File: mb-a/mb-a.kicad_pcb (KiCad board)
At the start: 2 copper layers, 39 x 56 mm, 29 parts, among them J1 Power, J2 Speaker, M1 Orange-Pi-Zero, U1 NCP1117-5.0_SOT223, U2 PAM8320, X1 I2C-6P

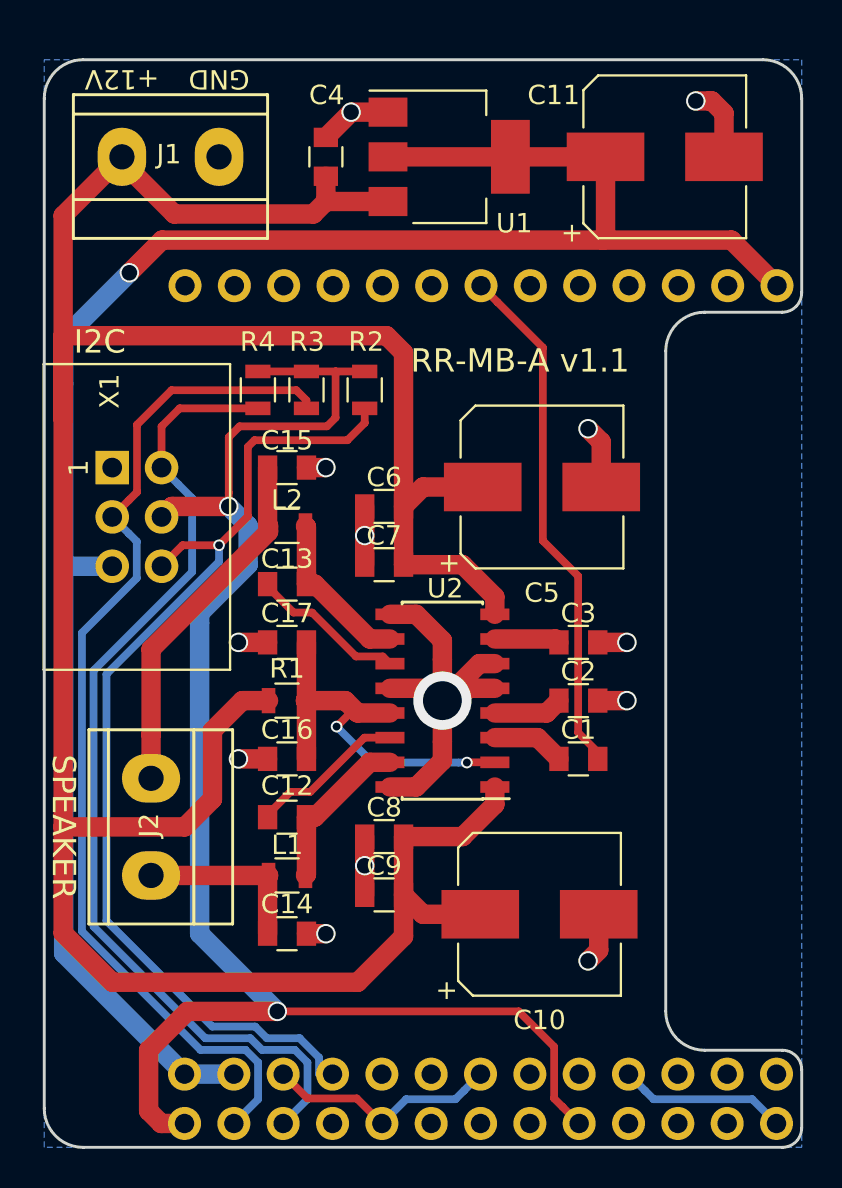
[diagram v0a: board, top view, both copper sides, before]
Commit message: Band switch support
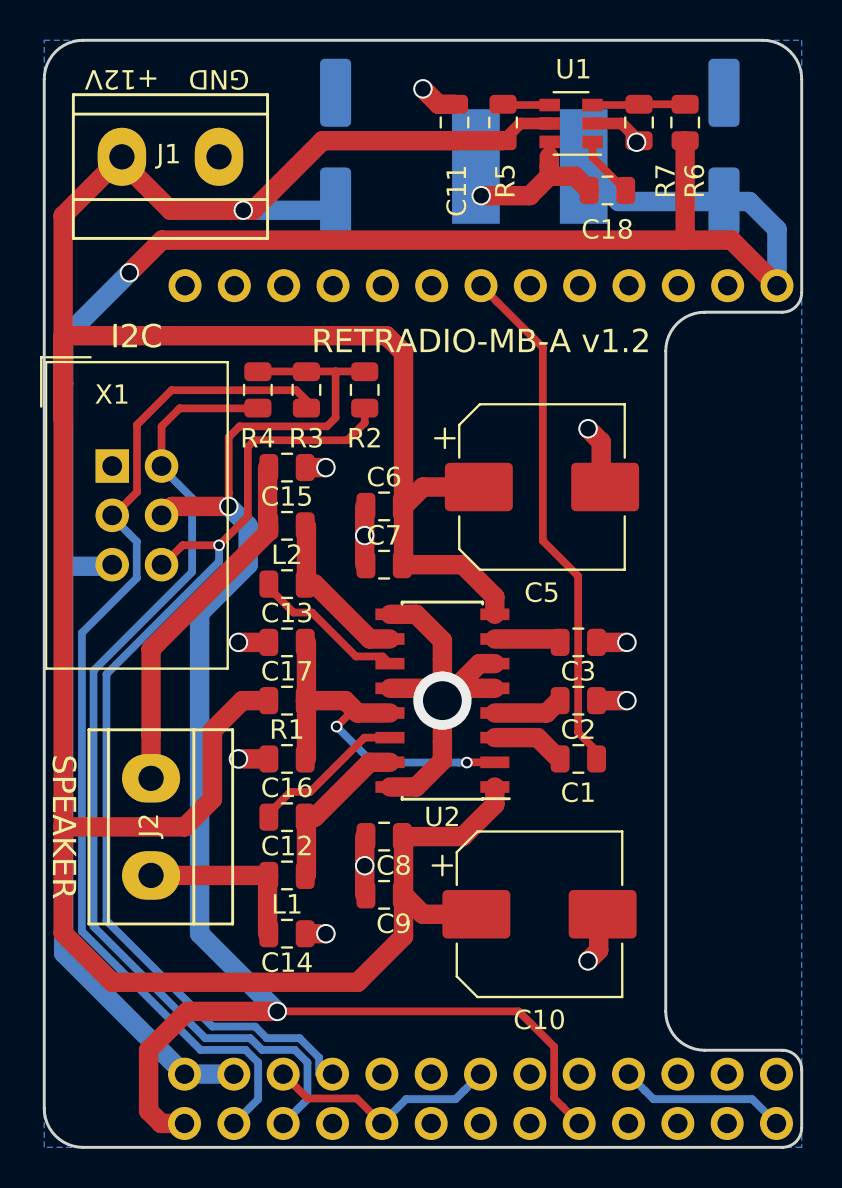
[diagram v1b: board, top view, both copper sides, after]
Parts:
- added C18: 100n, Capacitor_SMD:C_0805_2012Metric, F.Cu at (120.5, 46.7)
- added C19: 100u/12V, Capacitor_SMD:CP_Elec_6.3x5.4, B.Cu at (126.5, 44.5)
- added L3: 6.8uH, mb-a:L_Taiyo-Yuden_NR-60xx_HandSoldering, B.Cu at (116.5, 45.5)
- added R5: 100k, Resistor_SMD:R_0805_2012Metric, F.Cu at (115.1, 43.2)
- added R6: 30.9k 1%, Resistor_SMD:R_0805_2012Metric, F.Cu at (124.5, 43.2)
- added R7: 4.22k 1%, Resistor_SMD:R_0805_2012Metric, F.Cu at (122.1, 43.2)
- C1, C12, C13, C14, C15, C16, C17, C2, C3, C6, C7, C8, C9: footprint Capacitors_SMD:C_0805 -> Capacitor_SMD:C_0805_2012Metric
- C10, C5: footprint Capacitors_SMD:CP_Elec_8x10 -> Capacitor_SMD:CP_Elec_8x10
- C11: value 470u/16V -> 100n; footprint Capacitors_SMD:CP_Elec_8x10 -> Capacitor_SMD:C_0805_2012Metric
- C4: value 10u -> 100u/12V; footprint Capacitors_SMD:C_0805 -> Capacitor_SMD:CP_Elec_6.3x5.4; moved to B.Cu
- L1, L2: footprint Inductors_SMD:L_0805 -> Inductor_SMD:L_0805_2012Metric
- R1, R2, R3, R4: footprint Resistors_SMD:R_0805 -> Resistor_SMD:R_0805_2012Metric
- U1: value NCP1117-5.0_SOT223 -> FR8205; footprint TO_SOT_Packages_SMD:SOT-223-3Lead_TabPin2 -> Package_TO_SOT_SMD:SOT-23-6
- U2: footprint Housings_SOIC:SOIC-16_3.9x9.9mm_Pitch1.27mm -> Package_SO:SOIC-16_3.9x9.9mm_P1.27mm
- X1: footprint Connectors:IDC_Header_Straight_6pins -> Connector_IDC:IDC-Header_2x03_P2.54mm_Vertical
- moved C11 11.0 mm to (112.6, 43.2), turned to 270 degrees
- moved U1 6.51 mm to (118.6, 43.3), turned to 180 degrees
- moved C4 0.71 mm to (106.5, 44.5), turned to 90 degrees
- moved X1 0.08 mm to (95.0, 60.9), turned to 0 degrees
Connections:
- C11 pad 1: +5V -> GND
- C11 pad 2: GND -> +12V
- C4 pad 1: GND -> +12V
- C4 pad 2: +12V -> GND
- U1 pad 1: GND -> Net-(C18-Pad1)
- U1 pad 2: +5V -> GND
- U1 pad 3: +12V -> Net-(R6-Pad1)
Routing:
- net +12V: track 153.2 -> 166.7 mm, vias 0 -> 1
- net Net-(C18-Pad2): track 0.00 -> 8.78 mm, vias 0 -> 1
- net Net-(R6-Pad1): track 0.00 -> 4.79 mm
- net Net-(C18-Pad1): track 0.00 -> 3.21 mm
- net GND: track 70.7 -> 67.7 mm
- net +5V: track 101.8 -> 104.6 mm
- net Net-(R5-Pad1): track 0.00 -> 2.42 mm
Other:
- board size 39 x 56 mm -> 39 x 57 mm
- board text added: "RETRADIO-MB-A v1.2"
- board text removed: "RR-MB-A v1.1"
